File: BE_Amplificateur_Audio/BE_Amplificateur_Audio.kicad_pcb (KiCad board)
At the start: 2 copper layers, 110 x 100 mm, 52 parts, among them J2 Conn_01x02, J3 Conn_01x03, Q1 2N2907, Q10 TIP32, Q11 BD138, Q12 TIP31, Q13 2N2222, Q2 2N2907, Q3 2N2907, Q4 2N2222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

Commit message: MAJ jack down or side?
Is it possible to put the jack on the side?
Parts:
- moved U2 72.5 mm to (66.8, 121.4), turned to 90 degrees
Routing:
- net Net-(C1-Pad2): track 76.2 -> 10.4 mm
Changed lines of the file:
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@@
     (thickness 1.6)
     (drawings 6)
-    (tracks 249)
+    (tracks 248)
     (zones 0)
     (modules 52)
@@
     (32 B.Adhes user)
     (33 F.Adhes user)
-    (34 B.Paste user)
+    (34 B.Paste user hide)
     (35 F.Paste user)
-    (36 B.SilkS user)
+    (36 B.SilkS user hide)
     (37 F.SilkS user)
-    (38 B.Mask user)
+    (38 B.Mask user hide)
     (39 F.Mask user hide)
     (40 Dwgs.User user)
@@
   )
   (setup
-    (last_trace_width 2)
+    (last_trace_width 1.5)
     (user_trace_width 0.4)
     (user_trace_width 0.5)
@@
     (pad_to_mask_clearance 0.2)
     (aux_axis_origin 0 0)
-    (visible_elements FFFFFF7F)
+    (visible_elements 7FFFFFFF)
     (pcbplotparams
       (layerselection 0x010fc_ffffffff)
@@
   )
   (module Be-Elec:Jack_35RAPC2AV (layer F.Cu)
-    (at 136.8679 103.0859 180)
-    (fp_text reference U2 (at 1.1 6.7 180) (layer F.SilkS)
+    (at 66.76644 121.39168 90)
+    (fp_text reference U2 (at 1.1 6.7 90) (layer F.SilkS)
       (effects (font (size 1 1) (thickness 0.15)))
     )
-    (fp_text value Jack_Mono (at -0.8 -5.6 180) (layer F.Fab)
+    (fp_text value Jack_Mono (at -0.8 -5.6 90) (layer F.Fab)
       (effects (font (size 1 1) (thickness 0.15)))
     )
@@
     (fp_line (start 0 -3) (end -4 -3) (layer F.SilkS) (width 0.15))
     (fp_line (start 0 -3) (end 0 3) (layer F.SilkS) (width 0.15))
-    (fp_text user %R (at -4.3 6.6 180) (layer F.Fab)
+    (fp_text user %R (at -4.3 6.6 90) (layer F.Fab)
       (effects (font (size 1 1) (thickness 0.15)))
     )
-    (pad TN thru_hole circle (at 13.2 0 180) (size 3.5 3.5) (drill 2) (layers *.Cu *.Mask)
+    (pad TN thru_hole circle (at 13.2 0 90) (size 3.5 3.5) (drill 2) (layers *.Cu *.Mask)
       (net 32 "Net-(U2-PadTN)"))
-    (pad G thru_hole circle (at 2.1 0 180) (size 3.5 3.5) (drill 2) (layers *.Cu *.Mask)
+    (pad G thru_hole circle (at 2.1 0 90) (size 3.5 3.5) (drill 2) (layers *.Cu *.Mask)
       (net 7 GND))
-    (pad T thru_hole circle (at 7.4 0 180) (size 3.5 3.5) (drill 2) (layers *.Cu *.Mask)
+    (pad T thru_hole circle (at 7.4 0 90) (size 3.5 3.5) (drill 2) (layers *.Cu *.Mask)
       (net 2 "Net-(C1-Pad2)"))
   )
@@
   (segment (start 49.1998 103.6066) (end 41.9608 96.3676) (width 1.5) (layer B.Cu) (net 1))
   (segment (start 54.1655 103.6066) (end 49.1998 103.6066) (width 1.5) (layer B.Cu) (net 1))
-  (segment (start 61.3499 105.791) (end 67.8015 112.2426) (width 1.5) (layer B.Cu) (net 2))
-  (segment (start 67.8015 112.2426) (end 123.0249 112.2426) (width 1.5) (layer B.Cu) (net 2))
-  (segment (start 129.4679 105.7996) (end 129.4679 103.0859) (width 1.5) (layer B.Cu) (net 2))
-  (segment (start 123.0249 112.2426) (end 129.4679 105.7996) (width 1.5) (layer B.Cu) (net 2))
+  (segment (start 61.3499 108.57514) (end 66.76644 113.99168) (width 1.5) (layer B.Cu) (net 2))
+  (segment (start 61.3499 105.791) (end 61.3499 108.57514) (width 1.5) (layer B.Cu) (net 2))
   (segment (start 61.9252 61.8363) (end 64.4525 64.3636) (width 1.5) (layer B.Cu) (net 3))
   (segment (start 52.2986 61.8363) (end 61.9252 61.8363) (width 1.5) (layer B.Cu) (net 3))
@@
   (segment (start 96.5886 95.9088) (end 92.407199 91.727399) (width 1.5) (layer B.Cu) (net 3))
   (segment (start 92.407199 91.727399) (end 92.407199 83.643901) (width 1.5) (layer B.Cu) (net 3))
-  (segment (start 98.0186 97.4217) (end 98.0186 94.4088) (width 0.6) (layer B.Cu) (net 4))
-  (segment (start 77.9399 42.4434) (end 74.0664 46.3169) (width 1.5) (layer B.Cu) (net 5))
-  (segment (start 74.0664 46.3169) (end 74.0664 46.3677) (width 1.5) (layer B.Cu) (net 5))
-  (segment (start 73.0504 47.3837) (end 73.0504 48.7426) (width 1.5) (layer B.Cu) (net 5))
-  (segment (start 74.0664 46.3677) (end 73.0504 47.3837) (width 1.5) (layer B.Cu) (net 5))
-  (segment (start 77.9399 42.4434) (end 77.9399 42.4688) (width 1.5) (layer B.Cu) (net 5))
-  (segment (start 77.9399 42.4688) (end 81.8261 46.355) (width 1.5) (layer B.Cu) (net 5))
-  (segment (start 81.8261 46.355) (end 81.8261 53.8734) (width 1.5) (layer B.Cu) (net 5))
-  (segment (start 97.9932 68.2028) (end 97.9932 70.0824) (width 1.5) (layer B.Cu) (net 5))
-  (segment (start 98.0567 68.1393) (end 97.9932 68.2028) (width 1.5) (layer B.Cu) (net 5))
-  (segment (start 116.171262 51.342249) (end 116.171262 53.842249) (width 1.5) (layer B.Cu) (net 5))
-  (segment (start 117.513611 49.9999) (end 116.171262 51.342249) (width 1.5) (layer B.Cu) (net 5))
   (via (at 99.8474 78.6638) (size 1.9) (drill 0.6) (layers F.Cu B.Cu) (net 3))
   (via (at 106.210102 72.3392) (size 1.9) (drill 0.6) (layers F.Cu B.Cu) (net 3))
@@
   (segment (start 67.1449 67.056) (end 67.2084 67.056) (width 1.5) (layer B.Cu) (net 3))
   (via (at 84.6328 71.3613) (size 1.9) (drill 0.6) (layers F.Cu B.Cu) (net 3))
-  (segment (start 67.2084 67.056) (end 71.5137 71.3613) (width 1.5) (layer F.Cu) (net 3))
-  (segment (start 71.5137 71.3613) (end 83.289298 71.3613) (width 1.5) (layer F.Cu) (net 3))
-  (segment (start 83.289298 71.3613) (end 84.6328 71.3613) (width 1.5) (layer F.Cu) (net 3))
   (segment (start 85.4202 71.3613) (end 84.6328 71.3613) (width 1.5) (layer B.Cu) (net 3))
   (segment (start 94.2072 81.8439) (end 94.2072 80.1483) (width 1.5) (layer B.Cu) (net 3))
@@
   (segment (start 97.3873 78.6638) (end 99.8474 78.6638) (width 1.5) (layer B.Cu) (net 3))
   (segment (start 94.2072 81.8439) (end 97.3873 78.6638) (width 1.5) (layer B.Cu) (net 3))
+  (segment (start 83.289298 71.3613) (end 84.6328 71.3613) (width 1.5) (layer F.Cu) (net 3))
+  (segment (start 71.5645 71.3613) (end 83.289298 71.3613) (width 1.5) (layer F.Cu) (net 3))
+  (segment (start 67.2084 67.056) (end 67.2592 67.056) (width 1.5) (layer F.Cu) (net 3))
+  (segment (start 67.2592 67.056) (end 71.5645 71.3613) (width 1.5) (layer F.Cu) (net 3))
+  (segment (start 98.0186 97.4217) (end 98.0186 94.4088) (width 0.6) (layer B.Cu) (net 4))
   (segment (start 83.4136 100.838) (end 83.4136 105.0671) (width 1.5) (layer B.Cu) (net 4))
   (segment (start 56.6661 95.6453) (end 59.731799 98.710999) (width 1.5) (layer B.Cu) (net 4))
@@
   (segment (start 83.4136 105.0671) (end 84.4677 106.1212) (width 1.5) (layer B.Cu) (net 4))
   (segment (start 84.4677 106.1212) (end 94.1032 106.1212) (width 1.5) (layer B.Cu) (net 4))
+  (segment (start 77.9399 42.4434) (end 74.0664 46.3169) (width 1.5) (layer B.Cu) (net 5))
+  (segment (start 74.0664 46.3169) (end 74.0664 46.3677) (width 1.5) (layer B.Cu) (net 5))
+  (segment (start 73.0504 47.3837) (end 73.0504 48.7426) (width 1.5) (layer B.Cu) (net 5))
+  (segment (start 74.0664 46.3677) (end 73.0504 47.3837) (width 1.5) (layer B.Cu) (net 5))
+  (segment (start 77.9399 42.4434) (end 77.9399 42.4688) (width 1.5) (layer B.Cu) (net 5))
+  (segment (start 77.9399 42.4688) (end 81.8261 46.355) (width 1.5) (layer B.Cu) (net 5))
+  (segment (start 81.8261 46.355) (end 81.8261 53.8734) (width 1.5) (layer B.Cu) (net 5))
+  (segment (start 97.9932 68.2028) (end 97.9932 70.0824) (width 1.5) (layer B.Cu) (net 5))
+  (segment (start 98.0567 68.1393) (end 97.9932 68.2028) (width 1.5) (layer B.Cu) (net 5))
+  (segment (start 116.171262 51.342249) (end 116.171262 53.842249) (width 1.5) (layer B.Cu) (net 5))
+  (segment (start 117.513611 49.9999) (end 116.171262 51.342249) (width 1.5) (layer B.Cu) (net 5))
   (segment (start 76.6318 101.8032) (end 76.5175 101.8032) (width 1.5) (layer B.Cu) (net 5))
   (segment (start 98.3056 70.0824) (end 97.9932 70.0824) (width 1.5) (layer B.Cu) (net 5))

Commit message: PRET POUR VERIF
Problème de librairie de symboles qui est apparu --> résolu
Schematic à jour.
Netliste à jour.
Placement à jour.
Routage à jour.
Prêt pour vérification du placement et routage.
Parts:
- moved U2 72.5 mm to (136.9, 103.1), turned to 180 degrees
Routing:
- net Net-(C1-Pad2): track 10.4 -> 76.2 mm
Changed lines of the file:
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@@
     (thickness 1.6)
     (drawings 6)
-    (tracks 248)
+    (tracks 249)
     (zones 0)
     (modules 52)
@@
     (32 B.Adhes user)
     (33 F.Adhes user)
-    (34 B.Paste user hide)
+    (34 B.Paste user)
     (35 F.Paste user)
-    (36 B.SilkS user hide)
+    (36 B.SilkS user)
     (37 F.SilkS user)
-    (38 B.Mask user hide)
+    (38 B.Mask user)
     (39 F.Mask user hide)
     (40 Dwgs.User user)
@@
   )
   (setup
-    (last_trace_width 1.5)
+    (last_trace_width 0.4)
     (user_trace_width 0.4)
     (user_trace_width 0.5)
@@
   )
   (module Be-Elec:Jack_35RAPC2AV (layer F.Cu)
-    (at 66.76644 121.39168 90)
-    (fp_text reference U2 (at 1.1 6.7 90) (layer F.SilkS)
+    (at 136.8679 103.0859 180)
+    (fp_text reference U2 (at 1.1 6.7 180) (layer F.SilkS)
       (effects (font (size 1 1) (thickness 0.15)))
     )
-    (fp_text value Jack_Mono (at -0.8 -5.6 90) (layer F.Fab)
+    (fp_text value Jack_Mono (at -0.8 -5.6 180) (layer F.Fab)
       (effects (font (size 1 1) (thickness 0.15)))
     )
@@
     (fp_line (start 0 -3) (end -4 -3) (layer F.SilkS) (width 0.15))
     (fp_line (start 0 -3) (end 0 3) (layer F.SilkS) (width 0.15))
-    (fp_text user %R (at -4.3 6.6 90) (layer F.Fab)
+    (fp_text user %R (at -4.3 6.6 180) (layer F.Fab)
       (effects (font (size 1 1) (thickness 0.15)))
     )
-    (pad TN thru_hole circle (at 13.2 0 90) (size 3.5 3.5) (drill 2) (layers *.Cu *.Mask)
+    (pad TN thru_hole circle (at 13.2 0 180) (size 3.5 3.5) (drill 2) (layers *.Cu *.Mask)
       (net 32 "Net-(U2-PadTN)"))
-    (pad G thru_hole circle (at 2.1 0 90) (size 3.5 3.5) (drill 2) (layers *.Cu *.Mask)
+    (pad G thru_hole circle (at 2.1 0 180) (size 3.5 3.5) (drill 2) (layers *.Cu *.Mask)
       (net 7 GND))
-    (pad T thru_hole circle (at 7.4 0 90) (size 3.5 3.5) (drill 2) (layers *.Cu *.Mask)
+    (pad T thru_hole circle (at 7.4 0 180) (size 3.5 3.5) (drill 2) (layers *.Cu *.Mask)
       (net 2 "Net-(C1-Pad2)"))
   )
@@
   (segment (start 49.1998 103.6066) (end 41.9608 96.3676) (width 1.5) (layer B.Cu) (net 1))
   (segment (start 54.1655 103.6066) (end 49.1998 103.6066) (width 1.5) (layer B.Cu) (net 1))
-  (segment (start 61.3499 108.57514) (end 66.76644 113.99168) (width 1.5) (layer B.Cu) (net 2))
-  (segment (start 61.3499 105.791) (end 61.3499 108.57514) (width 1.5) (layer B.Cu) (net 2))
+  (segment (start 61.3499 105.791) (end 67.8015 112.2426) (width 1.5) (layer B.Cu) (net 2))
+  (segment (start 67.8015 112.2426) (end 123.0249 112.2426) (width 1.5) (layer B.Cu) (net 2))
+  (segment (start 129.4679 105.7996) (end 129.4679 103.0859) (width 1.5) (layer B.Cu) (net 2))
+  (segment (start 123.0249 112.2426) (end 129.4679 105.7996) (width 1.5) (layer B.Cu) (net 2))
   (segment (start 61.9252 61.8363) (end 64.4525 64.3636) (width 1.5) (layer B.Cu) (net 3))
   (segment (start 52.2986 61.8363) (end 61.9252 61.8363) (width 1.5) (layer B.Cu) (net 3))
@@
   (segment (start 67.1449 67.056) (end 67.2084 67.056) (width 1.5) (layer B.Cu) (net 3))
   (via (at 84.6328 71.3613) (size 1.9) (drill 0.6) (layers F.Cu B.Cu) (net 3))
+  (segment (start 67.2084 67.056) (end 71.5137 71.3613) (width 1.5) (layer F.Cu) (net 3))
+  (segment (start 71.5137 71.3613) (end 83.289298 71.3613) (width 1.5) (layer F.Cu) (net 3))
+  (segment (start 83.289298 71.3613) (end 84.6328 71.3613) (width 1.5) (layer F.Cu) (net 3))
   (segment (start 85.4202 71.3613) (end 84.6328 71.3613) (width 1.5) (layer B.Cu) (net 3))
   (segment (start 94.2072 81.8439) (end 94.2072 80.1483) (width 1.5) (layer B.Cu) (net 3))
@@
   (segment (start 97.3873 78.6638) (end 99.8474 78.6638) (width 1.5) (layer B.Cu) (net 3))
   (segment (start 94.2072 81.8439) (end 97.3873 78.6638) (width 1.5) (layer B.Cu) (net 3))
-  (segment (start 83.289298 71.3613) (end 84.6328 71.3613) (width 1.5) (layer F.Cu) (net 3))
-  (segment (start 71.5645 71.3613) (end 83.289298 71.3613) (width 1.5) (layer F.Cu) (net 3))
-  (segment (start 67.2084 67.056) (end 67.2592 67.056) (width 1.5) (layer F.Cu) (net 3))
-  (segment (start 67.2592 67.056) (end 71.5645 71.3613) (width 1.5) (layer F.Cu) (net 3))
   (segment (start 98.0186 97.4217) (end 98.0186 94.4088) (width 0.6) (layer B.Cu) (net 4))
   (segment (start 83.4136 100.838) (end 83.4136 105.0671) (width 1.5) (layer B.Cu) (net 4))

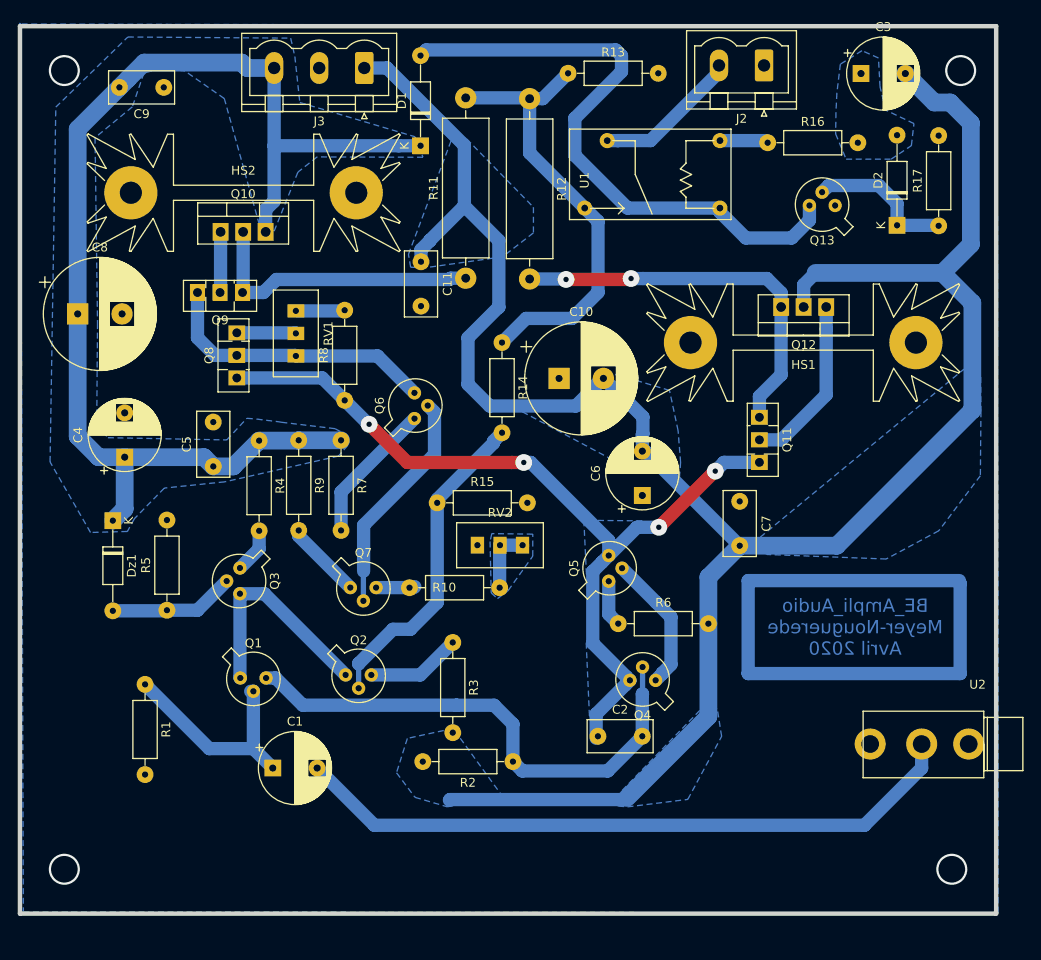
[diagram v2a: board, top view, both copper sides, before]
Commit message: Modifs après avis
Modifications après 1er avis de placement et routage
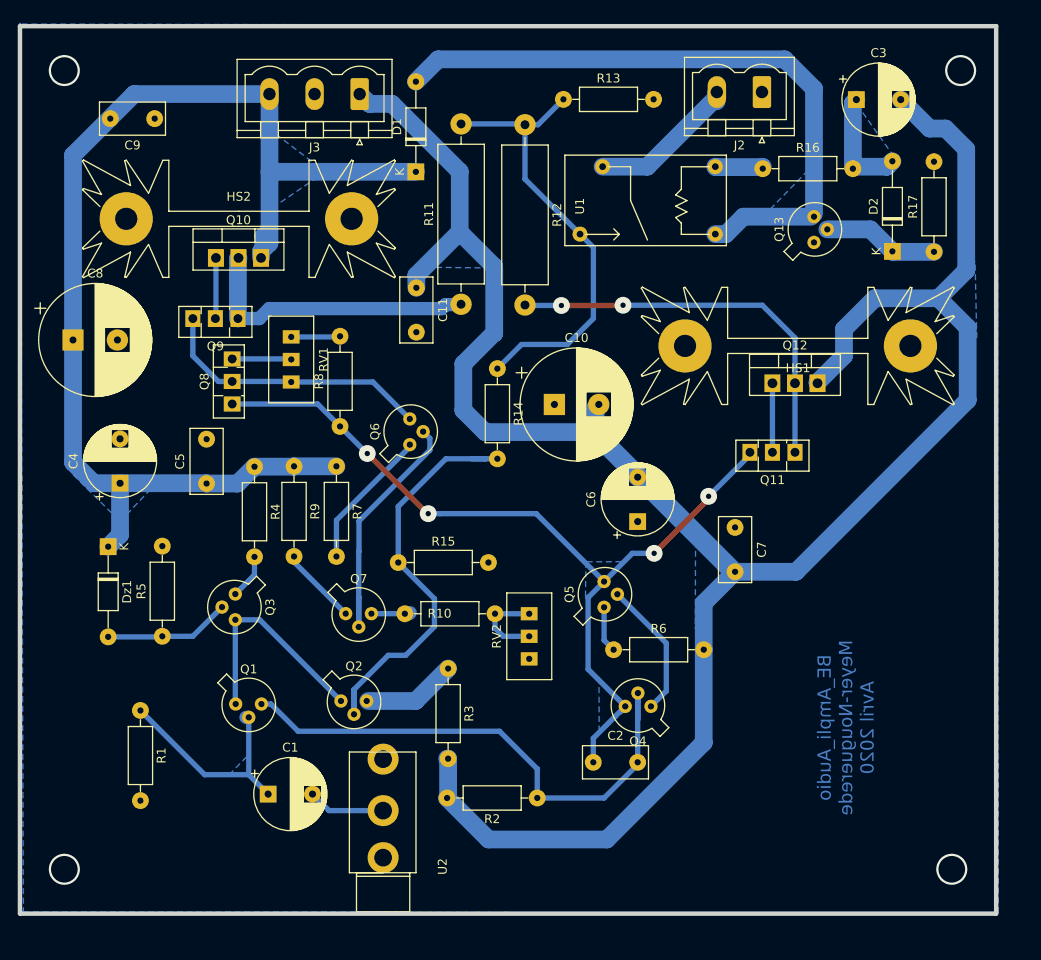
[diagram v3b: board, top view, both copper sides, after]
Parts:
- moved U2 69.7 mm to (68.8, 118.0), turned to 90 degrees
- moved Q12 10.5 mm to (112.7, 62.4), turned to 0 degrees
- moved R15 8.03 mm to (70.5, 82.6)
- moved RV2 7.76 mm to (85.2, 88.4), turned to 90 degrees
- moved Q11 5.62 mm to (115.2, 70.2), turned to 180 degrees
- moved R2 4.93 mm to (86.2, 109.2)
- moved Q13 4.56 mm to (117.4, 46.4), turned to 90 degrees
- moved C9 3.67 mm to (43.0, 32.6)
- moved J2 3.01 mm to (111.5, 29.6)
- moved C2 2.98 mm to (92.5, 105.1)
- moved C4 2.98 mm to (39.1, 73.7)
- moved Q5 2.98 mm to (93.8, 87.5)
- moved R3 2.98 mm to (76.1, 94.6)
- moved R4 2.98 mm to (54.3, 71.8)
- moved R7 2.98 mm to (63.5, 71.8)
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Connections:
- Q12 pad 2: -12V -> Net-(Q11-Pad1)
- Q12 pad 3: Net-(Q11-Pad1) -> -12V
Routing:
- net (no net): track 68.5 -> 0.00 mm
- net Net-(C1-Pad2): track 76.2 -> 8.73 mm
- net -12V: track 246.0 -> 272.3 mm
- net +12V: track 135.5 -> 148.7 mm
- net Net-(C3-Pad1): track 0.04 -> 12.5 mm
- net Net-(Q11-Pad2): track 19.5 -> 7.78 mm
- net Net-(Q2-Pad2): track 36.9 -> 48.6 mm
- net Net-(Q2-Pad3): track 10.7 -> 16.0 mm
- net Net-(D2-Pad1): track 16.8 -> 13.1 mm
- net Net-(Q6-Pad2): track 25.6 -> 29.0 mm
- net Net-(D1-Pad2): track 69.6 -> 73.0 mm
- net Net-(C2-Pad2): track 58.3 -> 61.3 mm
- net Net-(R10-Pad2): track 7.34 -> 9.71 mm
- net Net-(J2-Pad2): track 16.5 -> 17.8 mm
- net Net-(Q11-Pad1): track 44.1 -> 44.9 mm
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- added copper zone on B.Cu, net Net-(C1-Pad1)
- added copper zone on B.Cu, net Net-(D1-Pad2)
- removed copper zone on B.Cu, net Net-(R10-Pad2)

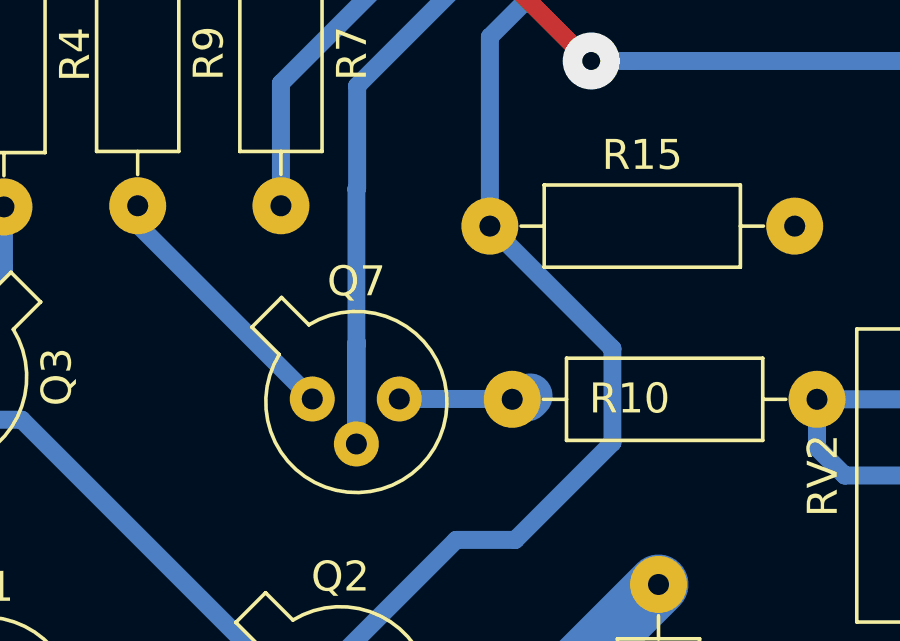
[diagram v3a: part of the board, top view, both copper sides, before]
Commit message: Corrections au niveau de Q7
J'ai corrigé les PWRFLAG et trouvé une erreur au niveau de Q7 : il manquait un fil. C'est corrigé et le routage est mis à jour.
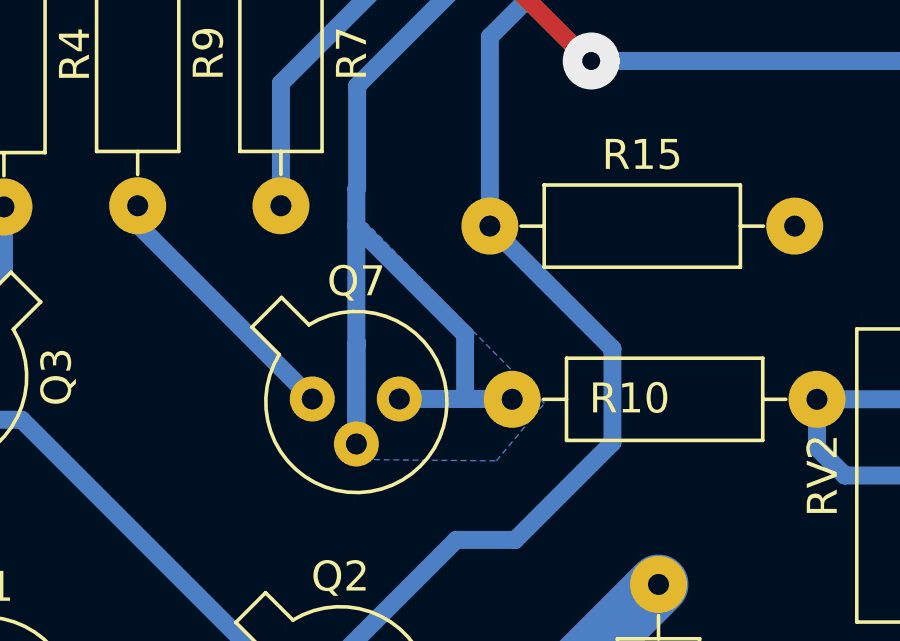
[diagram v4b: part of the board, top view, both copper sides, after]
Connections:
- Q7 pad 3: Net-(Q7-Pad3) -> Net-(Q6-Pad2)
- R10 pad 1: Net-(Q7-Pad3) -> Net-(Q6-Pad2)
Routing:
- net Net-(Q6-Pad2): track 29.0 -> 40.1 mm
- net Net-(Q7-Pad3): track 3.91 -> 0.00 mm
- added copper zone on B.Cu, net Net-(Q6-Pad2)
